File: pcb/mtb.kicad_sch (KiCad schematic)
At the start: 39 parts, among them J4 PROG/DEBUG, J5 pinheader, SW1 SW_MEC_5E, U10 L78L05_SOT89, U11 SN75176AP, U8 STM32F103C8Tx, U9 AMS1117-3.3, Y1 14,7456MHz

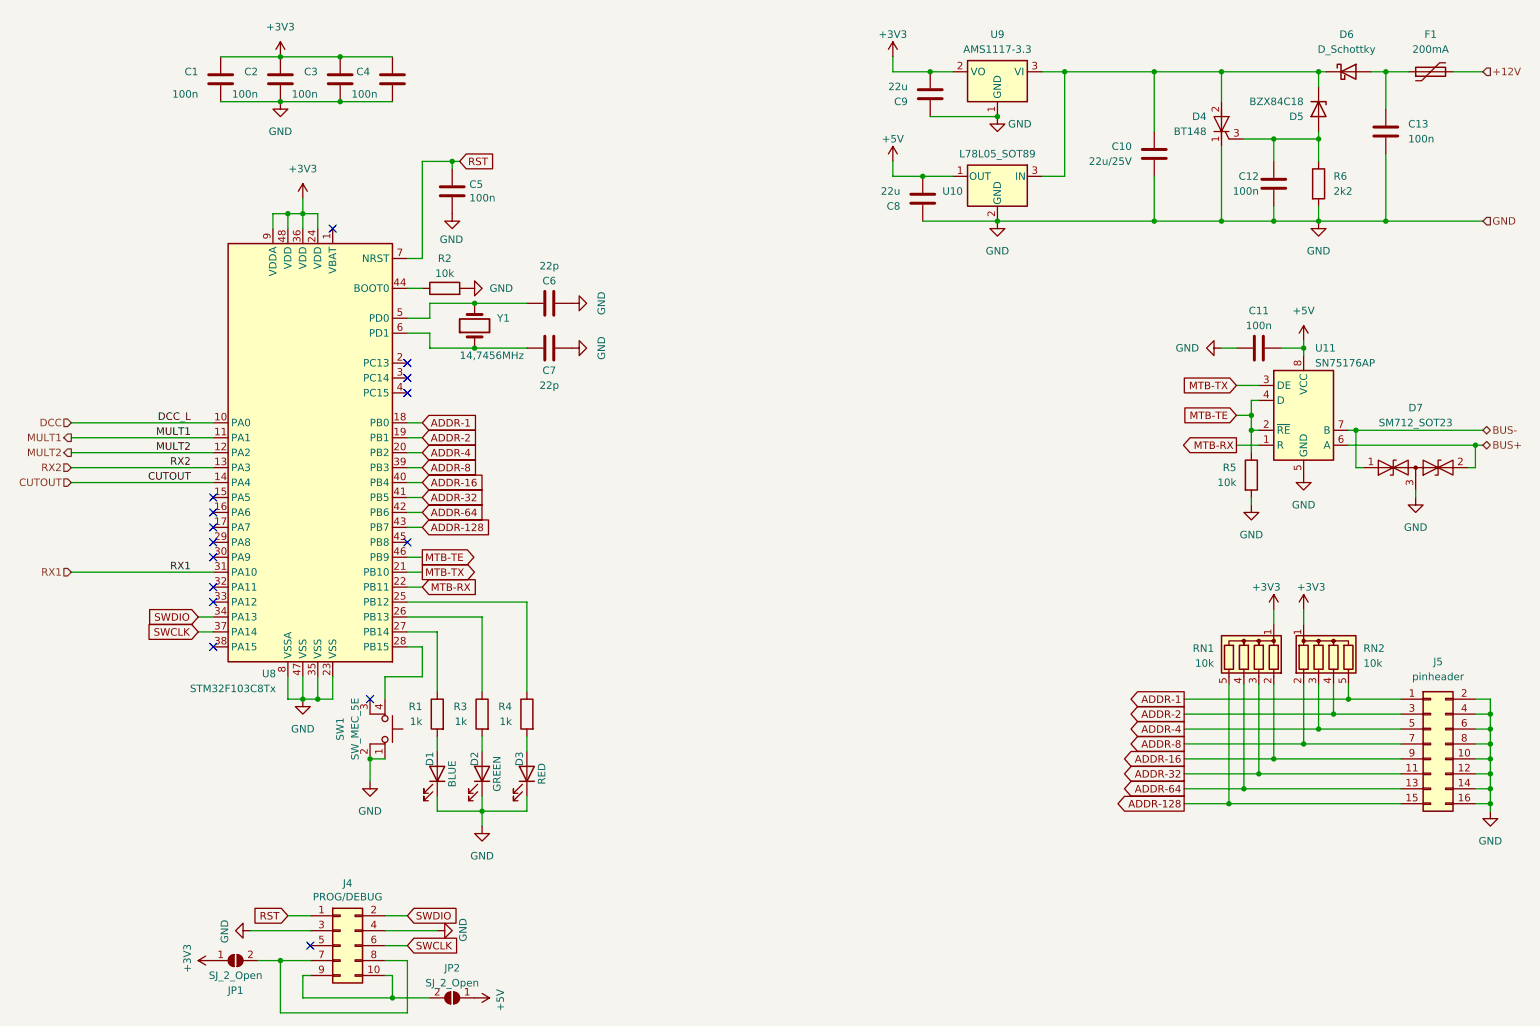
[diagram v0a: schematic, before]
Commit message: Added testpoints.
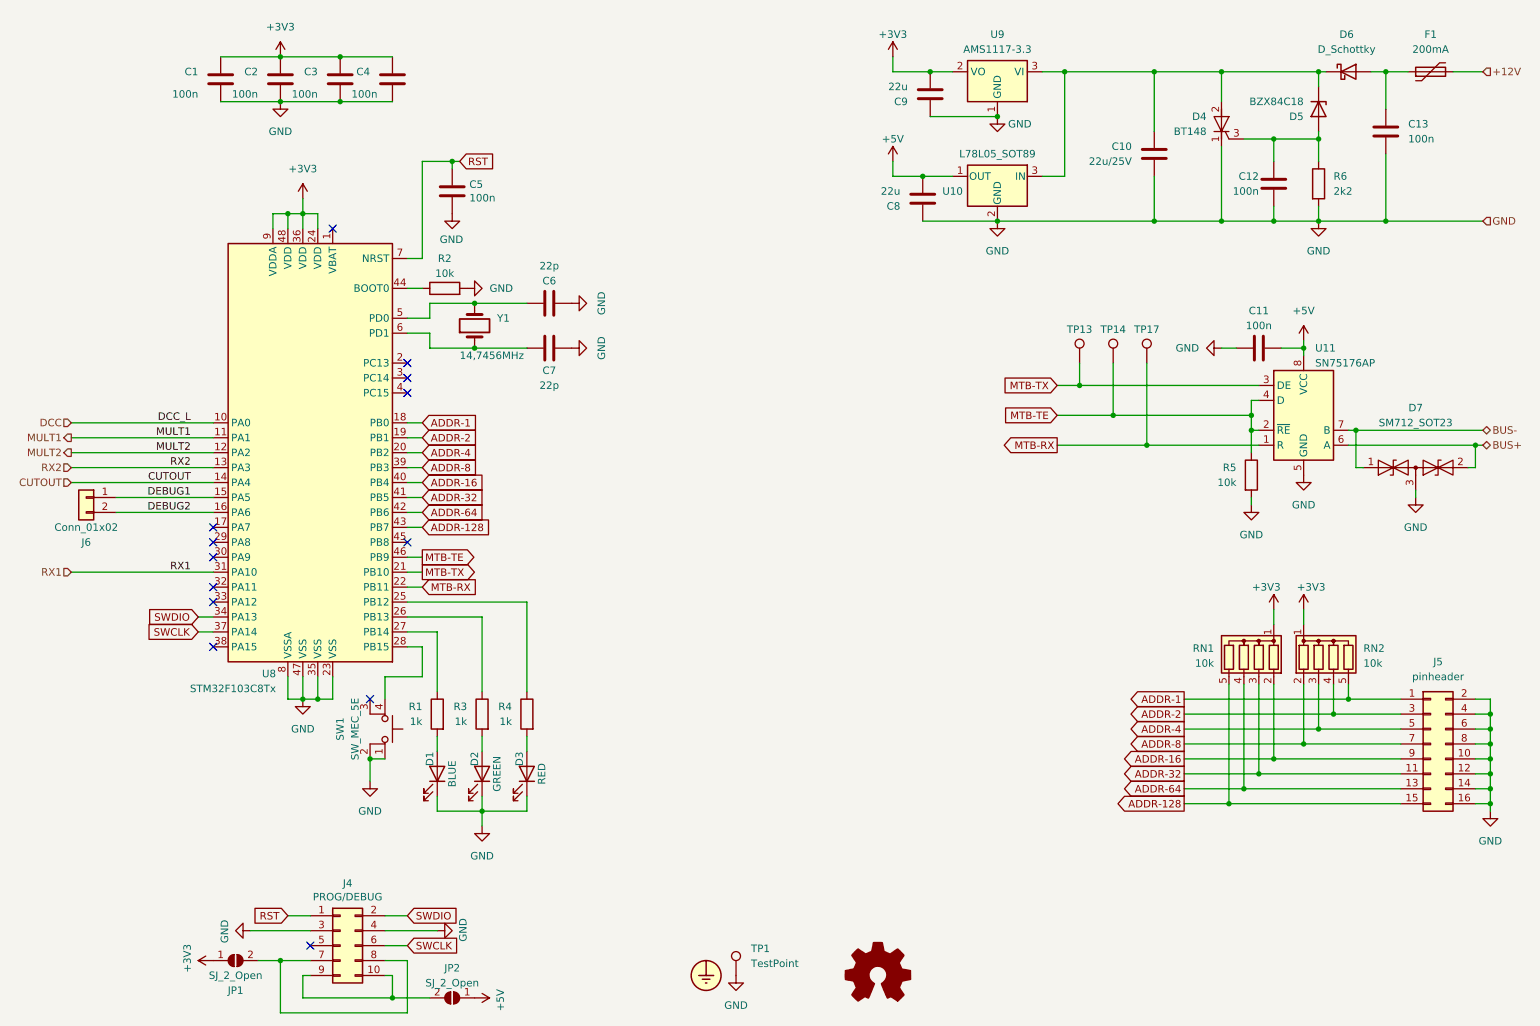
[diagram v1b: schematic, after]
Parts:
- added J6: Conn_01x02, symbol Connector_Generic:Conn_01x02
- added TP1, TP13, TP14, TP17: TestPoint, symbol Connector:TestPoint
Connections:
- net GND: now also TP1.1
- net MTB-RX: now also TP17.1
- net MTB-TE: now also TP14.1
- net MTB-TX: now also TP13.1
- net DEBUG1: now reaches U8.15 (PA5)
- net DEBUG1: now also J6.1 (Pin_1)
- net DEBUG2: now reaches U8.16 (PA6)
- net DEBUG2: now also J6.2 (Pin_2)
- no-connect marks 15 -> 13

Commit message: Make ERC PASS.
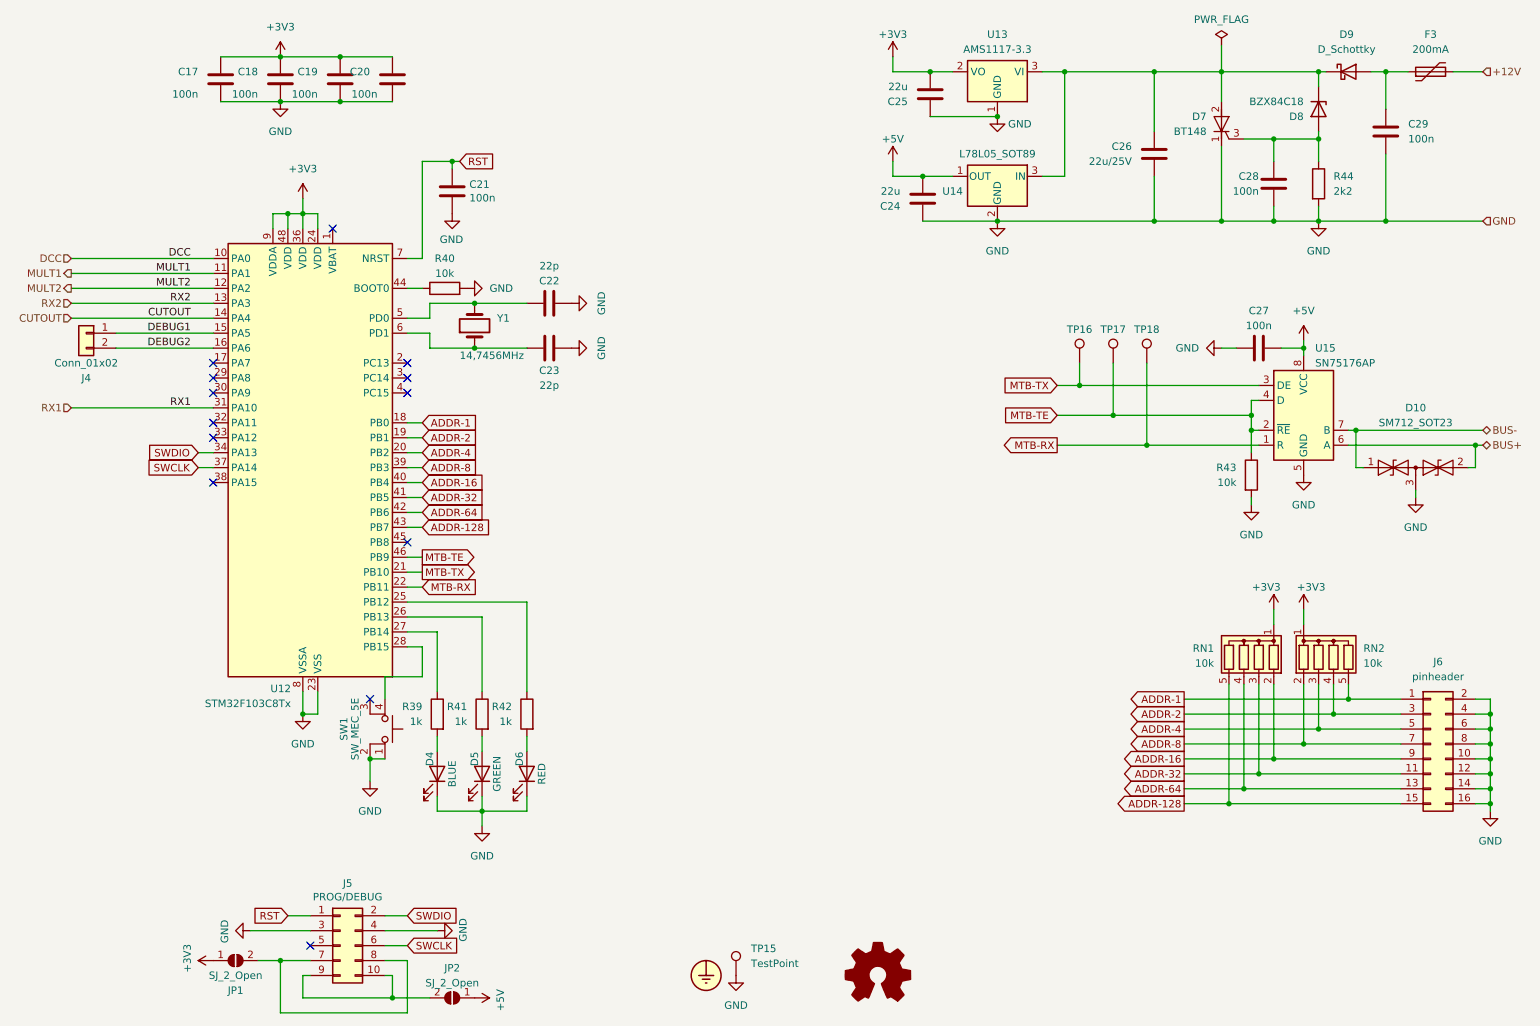
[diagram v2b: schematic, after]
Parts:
- renumbered C1 to C17, C2 to C18, C3 to C19, C4 to C20, C5 to C21, C6 to C22, C7 to C23, C8 to C24, C9 to C25, C10 to C26, C11 to C27, C12 to C28, C13 to C29, D7 to D10, D1 to D4, D2 to D5, D3 to D6, D4 to D7, D5 to D8, D6 to D9, F1 to F3, J6 to J4, J4 to J5, J5 to J6, R1 to R39, R2 to R40, R3 to R41, R4 to R42, R5 to R43, R6 to R44, TP1 to TP15, TP13 to TP16, TP14 to TP17, TP17 to TP18, U8 to U12, U9 to U13, U10 to U14, U11 to U15
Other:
- moved on the sheet: J4

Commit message: Added some footprints.
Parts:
- C17, C18, C19, C20, C22, C23, C24, C25, C26, C27, C28, C29: footprint (none) -> Capacitor_SMD:C_0805_2012Metric
- D4, D5, D6: footprint (none) -> LED_SMD:LED_0805_2012Metric
- D7: footprint (none) -> Package_TO_SOT_SMD:SOT-223
- J4: value Conn_01x02 -> PINHEADER; footprint (none) -> Connector_PinHeader_2.54mm:PinHeader_1x02_P2.54mm_Vertical
- J6: value pinheader -> PINHEADER; footprint (none) -> Connector_PinHeader_2.54mm:PinHeader_2x08_P2.54mm_Vertical
- R39, R40, R41, R42, R43, R44: footprint (none) -> Resistor_SMD:R_0805_2012Metric
- SW1: value SW_MEC_5E -> 6x6; footprint (none) -> Button_Switch_THT:SW_PUSH_6mm_H4.3mm
- TP15, TP16, TP17, TP18: value TestPoint -> PAD; footprint (none) -> TestPoint:TestPoint_Pad_D2.0mm
- U15: footprint Package_DIP:DIP-8_W7.62mm -> Package_DIP:DIP-8_W7.62mm_LongPads
- Y1: footprint (none) -> Crystal:Crystal_HC49-U_Vertical
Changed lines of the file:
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@@
       (effects (font (size 1.27 1.27)) (justify left))
     )
-    (property "Footprint" "" (at 232.7148 50.8 0)
+    (property "Footprint" "Capacitor_SMD:C_0805_2012Metric" (at 232.7148 50.8 0)
       (effects (font (size 1.27 1.27)) hide)
     )
@@
       (effects (font (size 1.27 1.27)))
     )
-    (property "Value" "TestPoint" (at 208.915 75.438 0)
+    (property "Value" "PAD" (at 208.915 75.438 0)
       (effects (font (size 1.27 1.27)) (justify left) hide)
     )
-    (property "Footprint" "" (at 211.455 77.47 0)
+    (property "Footprint" "TestPoint:TestPoint_Pad_D2.0mm" (at 211.455 77.47 0)
       (effects (font (size 1.27 1.27)) hide)
     )
@@
       (effects (font (size 1.27 1.27)) (justify left))
     )
-    (property "Footprint" "Package_DIP:DIP-8_W7.62mm" (at 238.76 99.06 0)
+    (property "Footprint" "Package_DIP:DIP-8_W7.62mm_LongPads" (at 238.76 99.06 0)
       (effects (font (size 1.27 1.27)) hide)
     )
@@
       (effects (font (size 1.27 1.27)) (justify left))
     )
-    (property "Footprint" "" (at 100.838 137.16 90)
+    (property "Footprint" "Resistor_SMD:R_0805_2012Metric" (at 100.838 137.16 90)
       (effects (font (size 1.27 1.27)) hide)
     )
@@
       (effects (font (size 1.27 1.27)))
     )
-    (property "Value" "TestPoint" (at 203.2 75.438 0)
+    (property "Value" "PAD" (at 203.2 75.438 0)
       (effects (font (size 1.27 1.27)) (justify left) hide)
     )
-    (property "Footprint" "" (at 205.74 77.47 0)
+    (property "Footprint" "TestPoint:TestPoint_Pad_D2.0mm" (at 205.74 77.47 0)
       (effects (font (size 1.27 1.27)) hide)
     )
@@
       (effects (font (size 1.27 1.27)) (justify left))
     )
-    (property "Value" "TestPoint" (at 144.78 179.578 0)
-      (effects (font (size 1.27 1.27)) (justify left))
-    )
-    (property "Footprint" "" (at 147.32 181.61 0)
+    (property "Value" "PAD" (at 144.78 179.578 0)
+      (effects (font (size 1.27 1.27)) (justify left))
+    )
+    (property "Footprint" "TestPoint:TestPoint_Pad_D2.0mm" (at 147.32 181.61 0)
       (effects (font (size 1.27 1.27)) hide)
     )
@@
       (effects (font (size 1.27 1.27)) (justify right))
     )
-    (property "Footprint" "" (at 214.3252 45.72 0)
+    (property "Footprint" "Capacitor_SMD:C_0805_2012Metric" (at 214.3252 45.72 0)
       (effects (font (size 1.27 1.27)) hide)
     )
@@
       (effects (font (size 1.27 1.27)) (justify right))
     )
-    (property "Footprint" "" (at 176.2252 27.94 0)
+    (property "Footprint" "Capacitor_SMD:C_0805_2012Metric" (at 176.2252 27.94 0)
       (effects (font (size 1.27 1.27)) hide)
     )
@@
       (effects (font (size 1.27 1.27)) (justify left))
     )
-    (property "Footprint" "" (at 239.522 46.99 90)
+    (property "Footprint" "Resistor_SMD:R_0805_2012Metric" (at 239.522 46.99 90)
       (effects (font (size 1.27 1.27)) hide)
     )
@@
       (effects (font (size 1.27 1.27)))
     )
-    (property "Value" "pinheader" (at 261.62 130.81 0)
-      (effects (font (size 1.27 1.27)))
-    )
-    (property "Footprint" "" (at 260.35 142.24 0)
+    (property "Value" "PINHEADER" (at 261.62 130.81 0)
+      (effects (font (size 1.27 1.27)))
+    )
+    (property "Footprint" "Connector_PinHeader_2.54mm:PinHeader_2x08_P2.54mm_Vertical" (at 260.35 142.24 0)
       (effects (font (size 1.27 1.27)) hide)
     )
@@
       (effects (font (size 1.27 1.27)))
     )
-    (property "Footprint" "" (at 99.06 147.32 0)
+    (property "Footprint" "LED_SMD:LED_0805_2012Metric" (at 99.06 147.32 0)
       (effects (font (size 1.27 1.27)) hide)
     )
@@
       (effects (font (size 1.27 1.27)) (justify right))
     )
-    (property "Footprint" "" (at 174.9552 45.72 0)
+    (property "Footprint" "Capacitor_SMD:C_0805_2012Metric" (at 174.9552 45.72 0)
       (effects (font (size 1.27 1.27)) hide)
     )
@@
       (effects (font (size 1.27 1.27)))
     )
-    (property "Footprint" "" (at 106.68 147.32 0)
+    (property "Footprint" "LED_SMD:LED_0805_2012Metric" (at 106.68 147.32 0)
       (effects (font (size 1.27 1.27)) hide)
     )
@@
       (effects (font (size 1.27 1.27)) (justify right))
     )
-    (property "Footprint" "" (at 97.79 71.12 0)
+    (property "Footprint" "Crystal:Crystal_HC49-U_Vertical" (at 97.79 71.12 0)
       (effects (font (size 1.27 1.27)) hide)
     )
@@
       (effects (font (size 1.27 1.27)))
     )
-    (property "Footprint" "" (at 227.33 75.8952 0)
+    (property "Footprint" "Capacitor_SMD:C_0805_2012Metric" (at 227.33 75.8952 0)
       (effects (font (size 1.27 1.27)) hide)
     )
@@
       (effects (font (size 1.27 1.27)) (justify left))
     )
-    (property "Footprint" "" (at 224.79 36.83 90)
+    (property "Footprint" "Package_TO_SOT_SMD:SOT-223" (at 224.79 36.83 90)
       (effects (font (size 1.27 1.27)) hide)
     )
@@
       (effects (font (size 1.27 1.27)) (justify left))
     )
-    (property "Footprint" "" (at 53.6448 33.02 0)
+    (property "Footprint" "Capacitor_SMD:C_0805_2012Metric" (at 53.6448 33.02 0)
       (effects (font (size 1.27 1.27)) hide)
     )
@@
       (effects (font (size 1.27 1.27)))
     )
-    (property "Footprint" "" (at 92.71 66.548 90)
+    (property "Footprint" "Resistor_SMD:R_0805_2012Metric" (at 92.71 66.548 90)
       (effects (font (size 1.27 1.27)) hide)
     )
@@
       (effects (font (size 1.27 1.27)))
     )
-    (property "Footprint" "" (at 114.3 66.3448 0)
+    (property "Footprint" "Capacitor_SMD:C_0805_2012Metric" (at 114.3 66.3448 0)
       (effects (font (size 1.27 1.27)) hide)
     )
@@
       (effects (font (size 1.27 1.27)))
     )
-    (property "Value" "TestPoint" (at 214.63 75.438 0)
+    (property "Value" "PAD" (at 214.63 75.438 0)
       (effects (font (size 1.27 1.27)) (justify left) hide)
     )
-    (property "Footprint" "" (at 217.17 77.47 0)
+    (property "Footprint" "TestPoint:TestPoint_Pad_D2.0mm" (at 217.17 77.47 0)
       (effects (font (size 1.27 1.27)) hide)
     )
@@
       (effects (font (size 1.27 1.27)) (justify left))
     )
-    (property "Footprint" "" (at 73.9648 33.02 0)
+    (property "Footprint" "Capacitor_SMD:C_0805_2012Metric" (at 73.9648 33.02 0)
       (effects (font (size 1.27 1.27)) hide)
     )
@@
       (effects (font (size 1.27 1.27)) (justify left))
     )
-    (property "Footprint" "" (at 253.6952 41.91 0)
+    (property "Footprint" "Capacitor_SMD:C_0805_2012Metric" (at 253.6952 41.91 0)
       (effects (font (size 1.27 1.27)) hide)
     )
@@
       (effects (font (size 1.27 1.27)) (justify left))
     )
-    (property "Footprint" "" (at 82.8548 33.02 0)
+    (property "Footprint" "Capacitor_SMD:C_0805_2012Metric" (at 82.8548 33.02 0)
       (effects (font (size 1.27 1.27)) hide)
     )
@@
       (effects (font (size 1.27 1.27)) (justify left))
     )
-    (property "Footprint" "" (at 93.218 137.16 90)
+    (property "Footprint" "Resistor_SMD:R_0805_2012Metric" (at 93.218 137.16 90)
       (effects (font (size 1.27 1.27)) hide)
     )
@@
       (effects (font (size 1.27 1.27)) (justify left))
     )
-    (property "Footprint" "" (at 63.8048 33.02 0)
+    (property "Footprint" "Capacitor_SMD:C_0805_2012Metric" (at 63.8048 33.02 0)
       (effects (font (size 1.27 1.27)) hide)
     )
@@
       (effects (font (size 1.27 1.27)) (justify left))
     )
-    (property "Footprint" "" (at 108.458 137.16 90)
+    (property "Footprint" "Resistor_SMD:R_0805_2012Metric" (at 108.458 137.16 90)
       (effects (font (size 1.27 1.27)) hide)
     )
@@
       (effects (font (size 1.27 1.27)))
     )
-    (property "Value" "Conn_01x02" (at 31.75 77.47 0)
-      (effects (font (size 1.27 1.27)))
-    )
-    (property "Footprint" "" (at 31.75 72.39 0)
+    (property "Value" "PINHEADER" (at 31.75 77.47 0)
+      (effects (font (size 1.27 1.27)))
+    )
+    (property "Footprint" "Connector_PinHeader_2.54mm:PinHeader_1x02_P2.54mm_Vertical" (at 31.75 72.39 0)
       (effects (font (size 1.27 1.27)) hide)
     )
@@
       (effects (font (size 1.27 1.27)))
     )
-    (property "Footprint" "" (at 91.44 147.32 0)
+    (property "Footprint" "LED_SMD:LED_0805_2012Metric" (at 91.44 147.32 0)
       (effects (font (size 1.27 1.27)) hide)
     )
@@
       (effects (font (size 1.27 1.27)) (justify right))
     )
-    (property "Footprint" "" (at 228.092 96.52 90)
+    (property "Footprint" "Resistor_SMD:R_0805_2012Metric" (at 228.092 96.52 90)
       (effects (font (size 1.27 1.27)) hide)
     )
@@
       (effects (font (size 1.27 1.27)))
     )
-    (property "Footprint" "" (at 114.3 73.9648 0)
+    (property "Footprint" "Capacitor_SMD:C_0805_2012Metric" (at 114.3 73.9648 0)
       (effects (font (size 1.27 1.27)) hide)
     )
@@
       (effects (font (size 1.27 1.27)))
     )
-    (property "Value" "SW_MEC_5E" (at 77.47 139.7 0)
-      (effects (font (size 1.27 1.27)))
-    )
-    (property "Footprint" "" (at 87.63 139.7 0)
-      (effects (font (size 1.27 1.27)) hide)
-    )
+    (property "Value" "6x6" (at 77.47 139.7 0)
+      (effects (font (size 1.27 1.27)))
+    )
+    (property "Footprint" "Button_Switch_THT:SW_PUSH_6mm_H4.3mm" (at 87.63 139.7 0)
+      (effects (font (size 1.27 1.27)) hide)
+    )
